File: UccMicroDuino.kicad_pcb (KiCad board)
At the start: 2 copper layers, 45.5 x 45 mm, 14 parts, among them J1 Pcb USB type A, J2 Header, U1 ATtiny85-20S

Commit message: Mi primer cambio para el practico 2
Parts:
- removed the D3 at (185.0, 86.3)
- removed D4: Led green, ledSmd:ledSMD
- removed R2, R3: 68Ω 5% 1/8W, Resistor_SMD:R_0805_2012Metric_Pad1.20x1.40mm_HandSolder
- removed R4, R5: 330Ω 5% 1/8W, Resistor_SMD:R_0805_2012Metric_Pad1.20x1.40mm_HandSolder
- D2: value 3.6V 1/2 mW -> D_Zener
- D3: renamed from D5; value LED RED -> LED
- J1: renamed from J2; value Header -> Conn_01x10_Socket
- J2: renamed from J1; value Pcb USB type A -> USB_A
- R1: value 1.5KΩ 5% 1/8W -> R
- U1: footprint Package_SO:SOIC-8_5.3x5.3mm_P1.27mm -> Package_SO:SOIC-8W_5.3x5.3mm_P1.27mm
- moved U1 63.9 mm to (131.7, 82.2), turned to 0 degrees
- moved J1 62.2 mm to (124.1, 67.9), turned to 0 degrees
- moved D2 48.4 mm to (129.3, 90.7), turned to 0 degrees
- moved R1 44.9 mm to (138.6, 70.1), turned to 0 degrees
- moved C1 40.1 mm to (138.6, 67.1), turned to 0 degrees
- moved J2 35.6 mm to (132.0, 72.2), turned to 0 degrees
- moved D1 35.0 mm to (129.6, 87.3), turned to 0 degrees
- moved D3 34.4 mm to (135.9, 88.7), turned to 0 degrees
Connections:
- C1 pad 1: +5V -> unconnected-(C1-Pad1)
- C1 pad 2: GND -> unconnected-(C1-Pad2)
- D1 pad 2: Net-(D1-A) -> unconnected-(D1-A-Pad2)
- D2 pad 1: Net-(D2-K) -> unconnected-(D2-K-Pad1)
- D2 pad 2: GND -> unconnected-(D2-A-Pad2)
- D3 pad 1: Net-(D5-K) -> unconnected-(D3-K-Pad1)
- D3 pad 2: +5V -> unconnected-(D3-A-Pad2)
- J1 pad 1: +5V -> unconnected-(J1-Pin_1-Pad1)
- J1 pad 2: GND -> unconnected-(J1-Pin_2-Pad2)
- J1 pad 4: Net-(J2-Pin_4) -> unconnected-(J1-Pin_4-Pad4)
- J1 pad 5: Net-(D4-A) -> unconnected-(J1-Pin_5-Pad5)
- J1 pad 6: Net-(J2-Pin_6) -> unconnected-(J1-Pin_6-Pad6)
- J1 pad 7: Net-(J2-Pin_7) -> unconnected-(J1-Pin_7-Pad7)
- J1 pad 8: Net-(J2-Pin_8) -> unconnected-(J1-Pin_8-Pad8)
- J1 pad 9: Net-(J2-Pin_9) -> unconnected-(J1-Pin_9-Pad9)
- J2 pad 1: Net-(D1-A) -> unconnected-(J2-VBUS-Pad1)
- J2 pad 2: Net-(D2-K) -> unconnected-(J2-D--Pad2)
- J2 pad 3: Net-(D3-K) -> unconnected-(J2-D+-Pad3)
- J2 pad 4: GND -> unconnected-(J2-GND-Pad4)
- R1 pad 2: Net-(D2-K) -> unconnected-(R1-Pad2)
- U1 pad 1: Net-(J2-Pin_9) -> unconnected-(U1-~{RESET}/PB5-Pad1)
- U1 pad 2: Net-(J2-Pin_7) -> unconnected-(U1-XTAL1/PB3-Pad2)
- U1 pad 3: Net-(J2-Pin_8) -> unconnected-(U1-XTAL2/PB4-Pad3)
- U1 pad 4: GND -> unconnected-(U1-GND-Pad4)
- U1 pad 5: Net-(J2-Pin_4) -> unconnected-(U1-AREF/PB0-Pad5)
- U1 pad 6: Net-(D4-A) -> unconnected-(U1-PB1-Pad6)
- U1 pad 7: Net-(J2-Pin_6) -> unconnected-(U1-PB2-Pad7)
- U1 pad 8: +5V -> unconnected-(U1-VCC-Pad8)
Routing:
- net GND: track 157.3 -> 0.00 mm
- net +5V: track 55.4 -> 0.00 mm
- net Net-(D4-A): track 51.0 -> 0.00 mm
- net Net-(J2-Pin_8): track 36.3 -> 0.00 mm
- net Net-(J2-Pin_7): track 33.5 -> 0.00 mm
- net Net-(D2-K): track 29.3 -> 0.00 mm
- net Net-(D3-K): track 26.1 -> 0.00 mm
- net Net-(J2-Pin_4): track 13.4 -> 0.00 mm
- net Net-(D1-A): track 10.6 -> 0.00 mm
- net Net-(J2-Pin_6): track 7.85 -> 0.00 mm
- net Net-(J2-Pin_9): track 6.18 -> 0.00 mm
- net Net-(D5-K): track 3.20 -> 0.00 mm
- net Net-(D4-K): track 3.19 -> 0.00 mm
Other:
- board outline removed

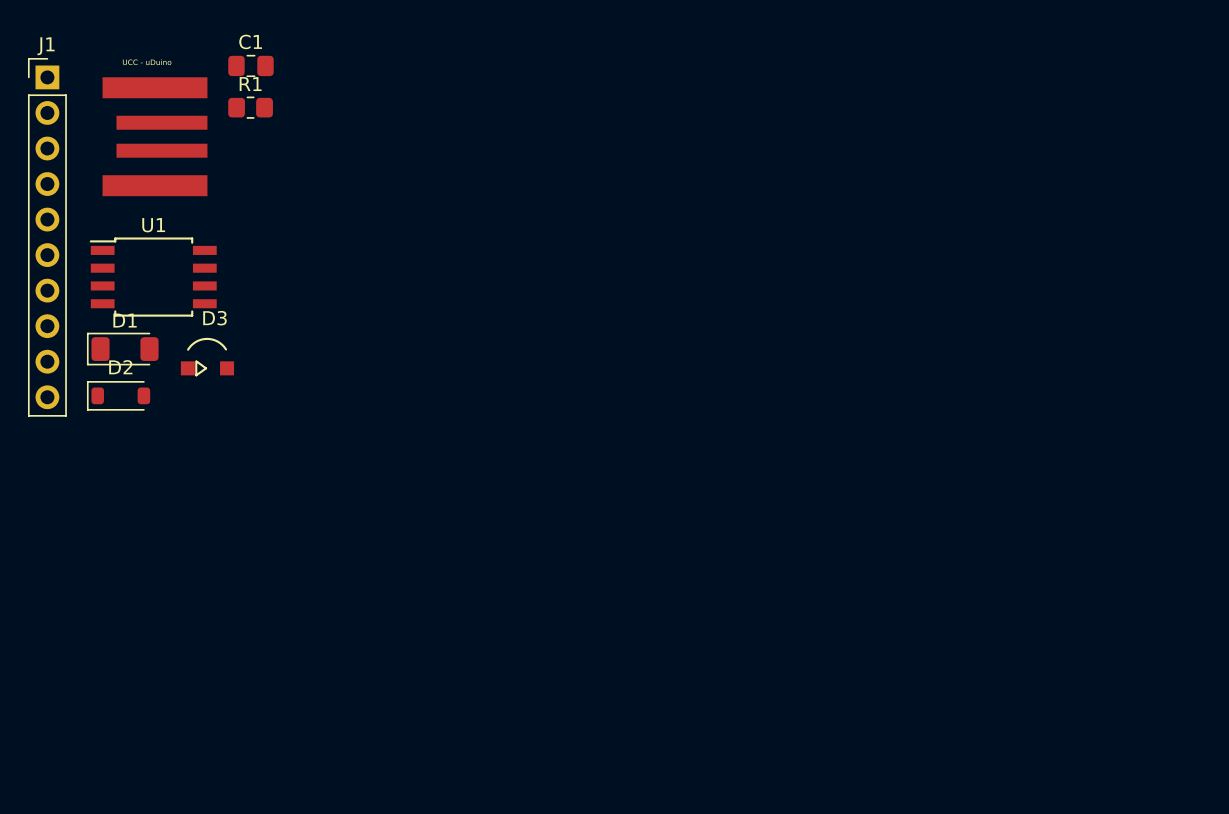
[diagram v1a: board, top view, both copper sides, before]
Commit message: Actualizando el PCB en la carpeta correcta
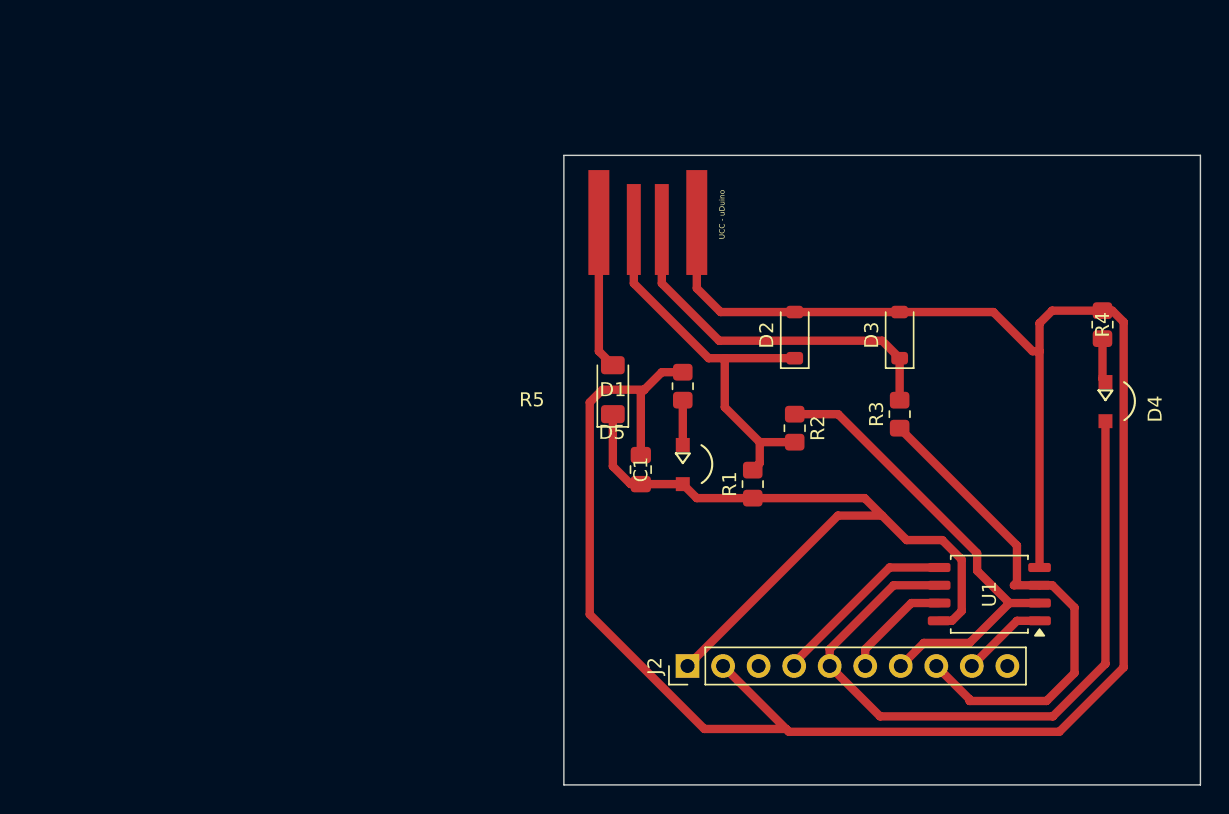
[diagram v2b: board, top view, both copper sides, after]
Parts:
- added D3: 3.6V 1/2 mW, Diode_SMD:D_SOD-123, F.Cu at (185.0, 86.3)
- added D4: Led green, ledSmd:ledSMD, F.Cu at (199.7, 91.5)
- added R2: 68Ω 5% 1/8W, Resistor_SMD:R_0805_2012Metric_Pad1.20x1.40mm_HandSolder, F.Cu at (177.5, 93.0)
- added R3: 68Ω 5% 1/8W, Resistor_SMD:R_0805_2012Metric_Pad1.20x1.40mm_HandSolder, F.Cu at (185.0, 92.0)
- added R4: 330Ω 5% 1/8W, Resistor_SMD:R_0805_2012Metric_Pad1.20x1.40mm_HandSolder, F.Cu at (199.5, 85.6)
- added R5: 330Ω 5% 1/8W, Resistor_SMD:R_0805_2012Metric_Pad1.20x1.40mm_HandSolder, F.Cu at (169.5, 90.0)
- D2: value D_Zener -> 3.6V 1/2 mW
- D5: renamed from D3; value LED -> LED RED
- J1: renamed from J2; value USB_A -> Pcb USB type A
- J2: renamed from J1; value Conn_01x10_Socket -> Header
- R1: value R -> 1.5KΩ 5% 1/8W
- U1: footprint Package_SO:SOIC-8W_5.3x5.3mm_P1.27mm -> Package_SO:SOIC-8_5.3x5.3mm_P1.27mm
- moved U1 63.9 mm to (191.4, 104.9), turned to 180 degrees
- moved J2 62.2 mm to (169.8, 110.0), turned to 90 degrees
- moved D2 48.4 mm to (177.5, 86.3), turned to 90 degrees
- moved R1 44.9 mm to (174.5, 97.0), turned to 90 degrees
- moved C1 40.1 mm to (166.5, 96.0), turned to 90 degrees
- moved J1 35.6 mm to (167.0, 78.5), turned to -90 degrees
- moved D1 35.0 mm to (164.5, 90.2), turned to 90 degrees
- moved D5 34.4 mm to (169.5, 96.0), turned to -90 degrees
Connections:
- C1 pad 1: unconnected-(C1-Pad1) -> +5V
- C1 pad 2: unconnected-(C1-Pad2) -> GND
- D1 pad 2: unconnected-(D1-A-Pad2) -> Net-(D1-A)
- D2 pad 1: unconnected-(D2-K-Pad1) -> Net-(D2-K)
- D2 pad 2: unconnected-(D2-A-Pad2) -> GND
- D5 pad 1: unconnected-(D3-K-Pad1) -> Net-(D5-K)
- D5 pad 2: unconnected-(D3-A-Pad2) -> +5V
- J1 pad 1: unconnected-(J2-VBUS-Pad1) -> Net-(D1-A)
- J1 pad 2: unconnected-(J2-D--Pad2) -> Net-(D2-K)
- J1 pad 3: unconnected-(J2-D+-Pad3) -> Net-(D3-K)
- J1 pad 4: unconnected-(J2-GND-Pad4) -> GND
- J2 pad 1: unconnected-(J1-Pin_1-Pad1) -> +5V
- J2 pad 2: unconnected-(J1-Pin_2-Pad2) -> GND
- J2 pad 4: unconnected-(J1-Pin_4-Pad4) -> Net-(J2-Pin_4)
- J2 pad 5: unconnected-(J1-Pin_5-Pad5) -> Net-(D4-A)
- J2 pad 6: unconnected-(J1-Pin_6-Pad6) -> Net-(J2-Pin_6)
- J2 pad 7: unconnected-(J1-Pin_7-Pad7) -> Net-(J2-Pin_7)
- J2 pad 8: unconnected-(J1-Pin_8-Pad8) -> Net-(J2-Pin_8)
- J2 pad 9: unconnected-(J1-Pin_9-Pad9) -> Net-(J2-Pin_9)
- R1 pad 2: unconnected-(R1-Pad2) -> Net-(D2-K)
- U1 pad 1: unconnected-(U1-~{RESET}/PB5-Pad1) -> Net-(J2-Pin_9)
- U1 pad 2: unconnected-(U1-XTAL1/PB3-Pad2) -> Net-(J2-Pin_7)
- U1 pad 3: unconnected-(U1-XTAL2/PB4-Pad3) -> Net-(J2-Pin_8)
- U1 pad 4: unconnected-(U1-GND-Pad4) -> GND
- U1 pad 5: unconnected-(U1-AREF/PB0-Pad5) -> Net-(J2-Pin_4)
- U1 pad 6: unconnected-(U1-PB1-Pad6) -> Net-(D4-A)
- U1 pad 7: unconnected-(U1-PB2-Pad7) -> Net-(J2-Pin_6)
- U1 pad 8: unconnected-(U1-VCC-Pad8) -> +5V
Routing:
- net GND: track 0.00 -> 157.3 mm
- net +5V: track 0.00 -> 55.4 mm
- net Net-(D4-A): track 0.00 -> 51.0 mm
- net Net-(J2-Pin_8): track 0.00 -> 36.3 mm
- net Net-(J2-Pin_7): track 0.00 -> 33.5 mm
- net Net-(D2-K): track 0.00 -> 29.3 mm
- net Net-(D3-K): track 0.00 -> 26.1 mm
- net Net-(J2-Pin_4): track 0.00 -> 13.4 mm
- net Net-(D1-A): track 0.00 -> 10.6 mm
- net Net-(J2-Pin_6): track 0.00 -> 7.85 mm
- net Net-(J2-Pin_9): track 0.00 -> 6.18 mm
- net Net-(D5-K): track 0.00 -> 3.20 mm
- net Net-(D4-K): track 0.00 -> 3.19 mm
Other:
- board outline added: 45.5 x 45 mm
